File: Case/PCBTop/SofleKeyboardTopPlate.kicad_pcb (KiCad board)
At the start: 2 copper layers, 137.2 x 109.2 mm, 5 parts

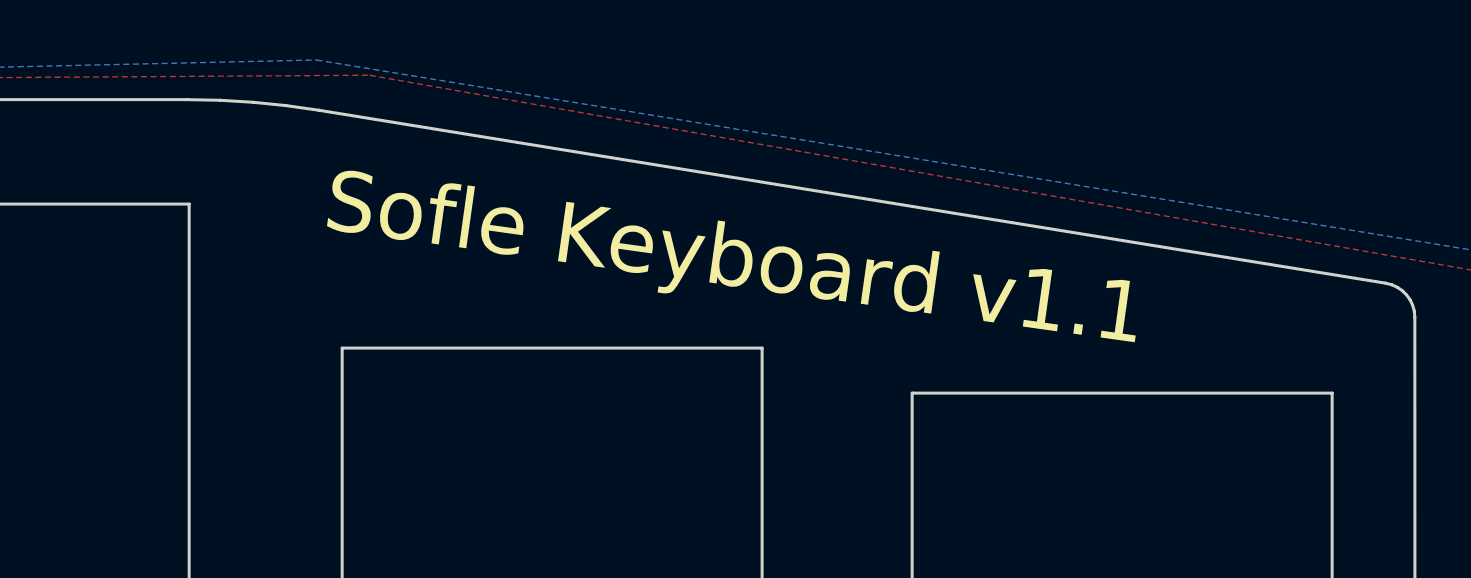
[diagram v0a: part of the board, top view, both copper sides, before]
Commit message: Changed labels on silk screens
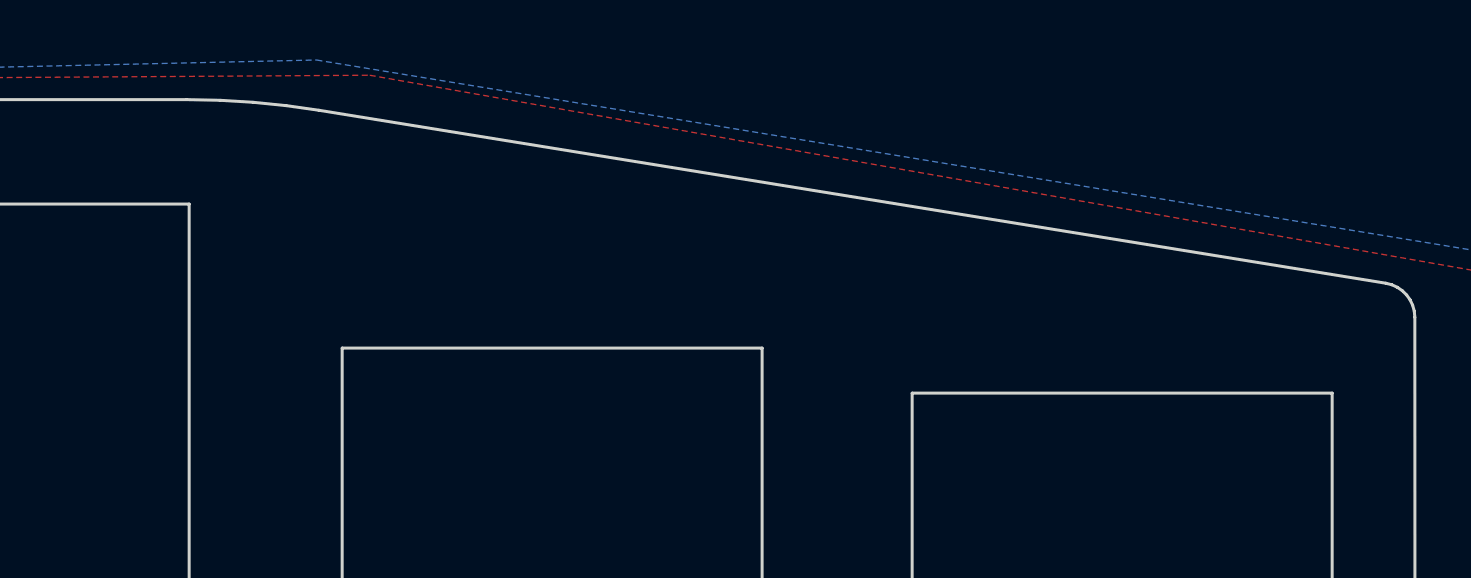
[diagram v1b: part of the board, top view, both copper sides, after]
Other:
- board text removed: "Sofle Keyboard v1.1"
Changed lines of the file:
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@@
-(kicad_pcb (version 20171130) (host pcbnew 5.1.5-52549c5~84~ubuntu19.04.1)
+(kicad_pcb (version 20171130) (host pcbnew 5.1.4-e60b266~84~ubuntu18.04.1)
   (general
     (thickness 1.6)
-    (drawings 352)
+    (drawings 350)
     (tracks 0)
     (zones 0)
@@
   (page A4)
   (layers
-    (0 F.Cu signal)
-    (31 B.Cu signal)
-    (32 B.Adhes user)
-    (33 F.Adhes user)
-    (34 B.Paste user)
-    (35 F.Paste user)
+    (0 F.Cu signal hide)
+    (31 B.Cu signal hide)
+    (32 B.Adhes user hide)
+    (33 F.Adhes user hide)
+    (34 B.Paste user hide)
+    (35 F.Paste user hide)
     (36 B.SilkS user)
-    (37 F.SilkS user)
-    (38 B.Mask user)
+    (37 F.SilkS user hide)
+    (38 B.Mask user hide)
     (39 F.Mask user)
-    (40 Dwgs.User user)
-    (41 Cmts.User user)
-    (42 Eco1.User user)
-    (43 Eco2.User user)
+    (40 Dwgs.User user hide)
+    (41 Cmts.User user hide)
+    (42 Eco1.User user hide)
+    (43 Eco2.User user hide)
     (44 Edge.Cuts user)
-    (45 Margin user)
-    (46 B.CrtYd user)
-    (47 F.CrtYd user)
-    (48 B.Fab user)
-    (49 F.Fab user)
+    (45 Margin user hide)
+    (46 B.CrtYd user hide)
+    (47 F.CrtYd user hide)
+    (48 B.Fab user hide)
+    (49 F.Fab user hide)
   )
   (setup
@@
     (pad 5 thru_hole circle (at 0 0) (size 4 4) (drill 2.2) (layers *.Cu *.Mask))
   )
-  (gr_text "Sofle Keyboard v1.1" (at 134.874 21.59 -8) (layer B.SilkS)
-    (effects (font (size 2 2) (thickness 0.3)) (justify mirror))
-  )
-  (gr_text "Sofle Keyboard v1.1" (at 134.874 21.844 -8) (layer F.SilkS)
-    (effects (font (size 2 2) (thickness 0.3)))
-  )
   (gr_line (start 156.48528 100.85732) (end 137.77211 102.3628) (layer Edge.Cuts) (width 0.1))
